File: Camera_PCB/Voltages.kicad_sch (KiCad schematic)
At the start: 29 parts

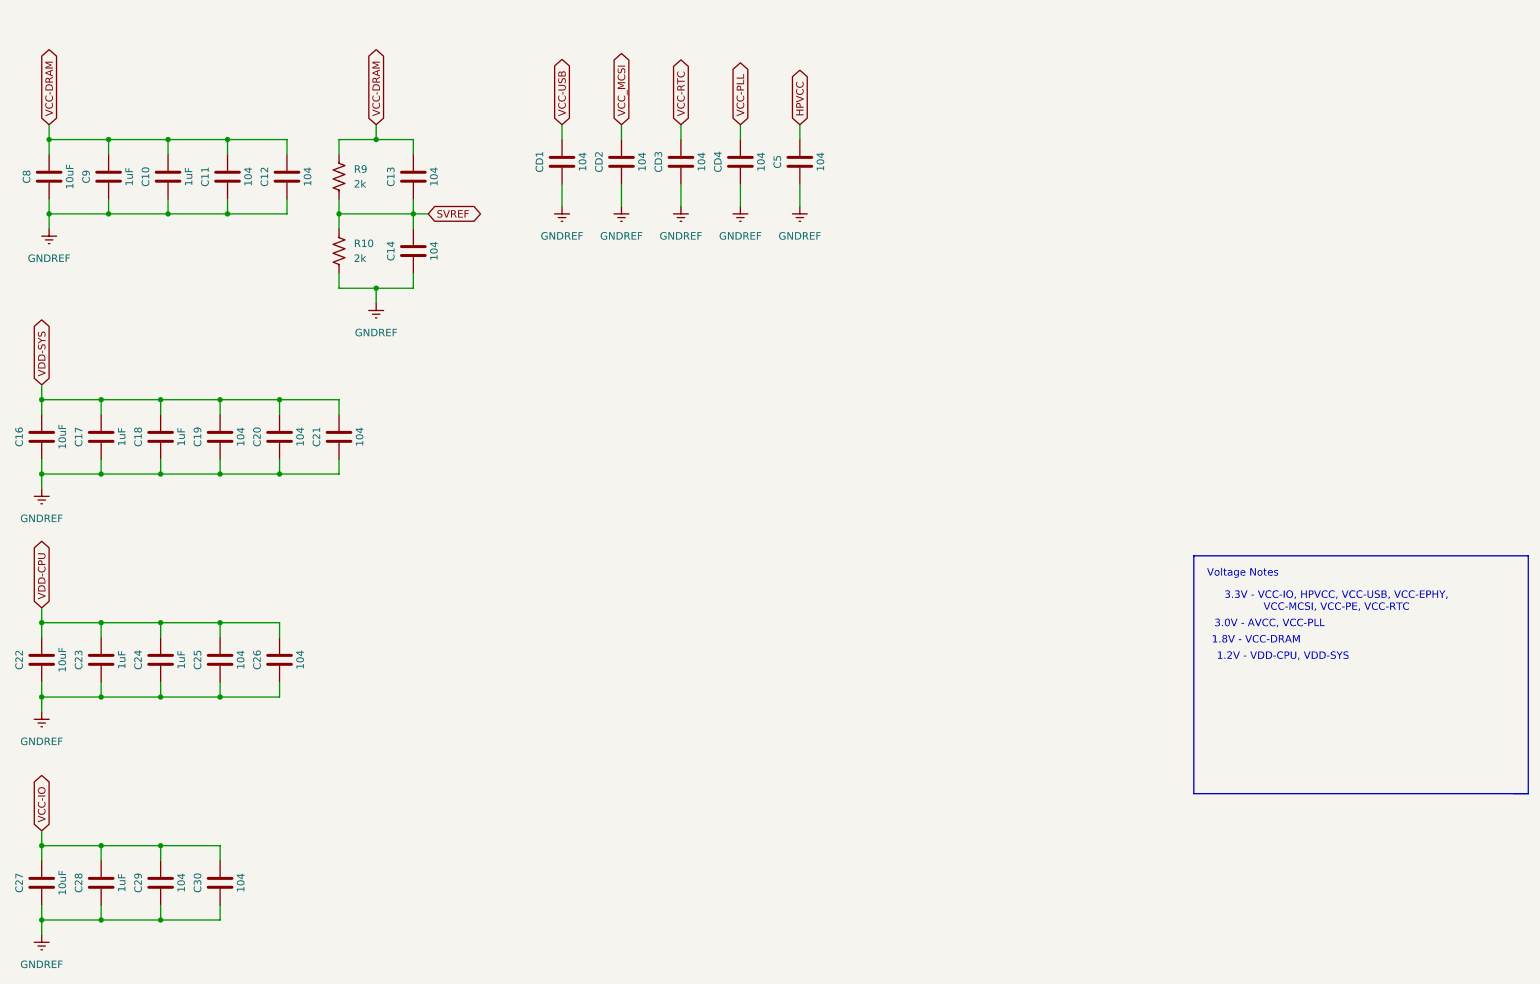
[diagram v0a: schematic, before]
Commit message: Fixed Capacitor Naming
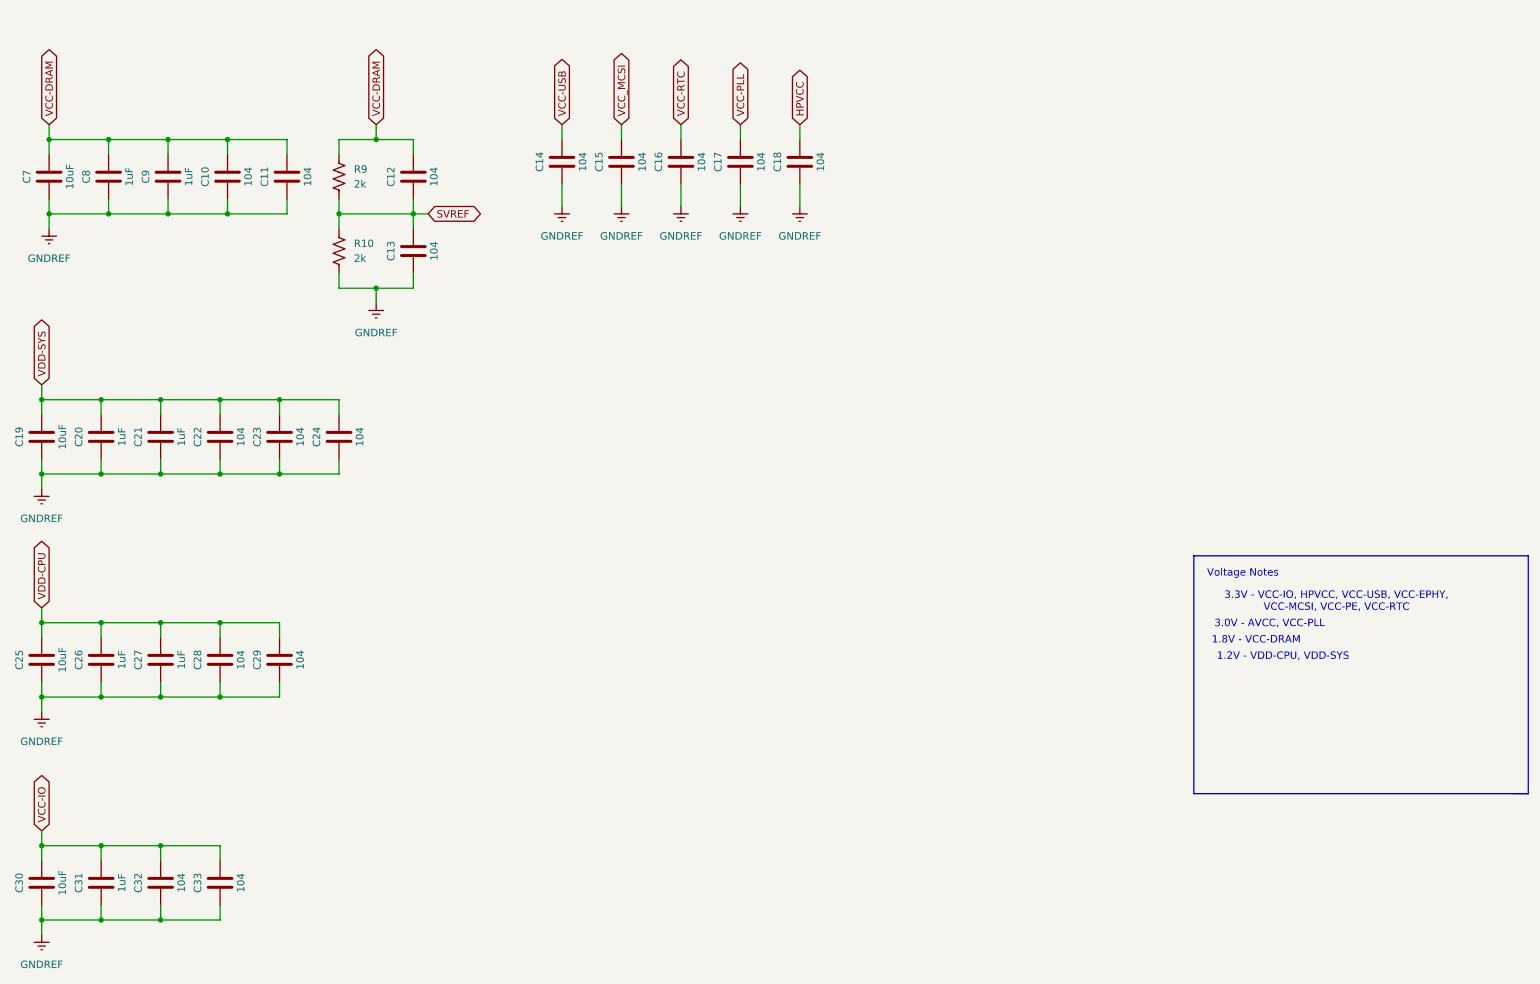
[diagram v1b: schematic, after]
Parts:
- renumbered C11 to C10, C12 to C11, C13 to C12, C14 to C13, CD1 to C14, CD2 to C15, CD3 to C16, CD4 to C17, C5 to C18, C16 to C19, C17 to C20, C18 to C21, C19 to C22, C20 to C23, C21 to C24, C22 to C25, C23 to C26, C24 to C27, C25 to C28, C26 to C29, C27 to C30, C28 to C31, C29 to C32, C30 to C33, C8 to C7, C9 to C8, C10 to C9
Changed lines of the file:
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@@
 		(on_board yes)
 		(dnp no)
-		(property "Reference" "C17"
+		(property "Reference" "C20"
 			(at 30.48 100.33 90)
 			(effects
@@
 			(project "Camera_PCB"
 				(path "/400c1603-202c-4359-a830-d2f0d06dd3ce/8aea63de-025a-40df-acd1-ce0de9a2cf46"
-					(reference "C17")
+					(reference "C20")
 					(unit 1)
 				)
@@
 		(on_board yes)
 		(dnp no)
-		(property "Reference" "CD1"
+		(property "Reference" "C14"
 			(at 109.22 53.34 90)
 			(effects
@@
 			(project "Camera_PCB"
 				(path "/400c1603-202c-4359-a830-d2f0d06dd3ce/8aea63de-025a-40df-acd1-ce0de9a2cf46"
-					(reference "CD1")
+					(reference "C14")
 					(unit 1)
 				)
@@
 		(on_board yes)
 		(dnp no)
-		(property "Reference" "C29"
+		(property "Reference" "C32"
 			(at 40.64 176.53 90)
 			(effects
@@
 			(project "Camera_PCB"
 				(path "/400c1603-202c-4359-a830-d2f0d06dd3ce/8aea63de-025a-40df-acd1-ce0de9a2cf46"
-					(reference "C29")
+					(reference "C32")
 					(unit 1)
 				)
@@
 		(on_board yes)
 		(dnp no)
-		(property "Reference" "C14"
+		(property "Reference" "C13"
 			(at 83.82 68.58 90)
 			(effects
@@
 			(project "Camera_PCB"
 				(path "/400c1603-202c-4359-a830-d2f0d06dd3ce/8aea63de-025a-40df-acd1-ce0de9a2cf46"
-					(reference "C14")
+					(reference "C13")
 					(unit 1)
 				)
@@
 		(on_board yes)
 		(dnp no)
-		(property "Reference" "C28"
+		(property "Reference" "C31"
 			(at 30.48 176.53 90)
 			(effects
@@
 			(project "Camera_PCB"
 				(path "/400c1603-202c-4359-a830-d2f0d06dd3ce/8aea63de-025a-40df-acd1-ce0de9a2cf46"
-					(reference "C28")
+					(reference "C31")
 					(unit 1)
 				)
@@
 		(on_board yes)
 		(dnp no)
-		(property "Reference" "CD4"
+		(property "Reference" "C17"
 			(at 139.7 53.34 90)
 			(effects
@@
 			(project "Camera_PCB"
 				(path "/400c1603-202c-4359-a830-d2f0d06dd3ce/8aea63de-025a-40df-acd1-ce0de9a2cf46"
-					(reference "CD4")
+					(reference "C17")
 					(unit 1)
 				)
@@
 		(on_board yes)
 		(dnp no)
-		(property "Reference" "C11"
+		(property "Reference" "C10"
 			(at 52.07 55.88 90)
 			(effects
@@
 			(project "Camera_PCB"
 				(path "/400c1603-202c-4359-a830-d2f0d06dd3ce/8aea63de-025a-40df-acd1-ce0de9a2cf46"
-					(reference "C11")
+					(reference "C10")
 					(unit 1)
 				)
@@
 		(on_board yes)
 		(dnp no)
-		(property "Reference" "C22"
+		(property "Reference" "C25"
 			(at 20.32 138.43 90)
 			(effects
@@
 			(project "Camera_PCB"
 				(path "/400c1603-202c-4359-a830-d2f0d06dd3ce/8aea63de-025a-40df-acd1-ce0de9a2cf46"
-					(reference "C22")
+					(reference "C25")
 					(unit 1)
 				)
@@
 		(on_board yes)
 		(dnp no)
-		(property "Reference" "C30"
+		(property "Reference" "C33"
 			(at 50.8 176.53 90)
 			(effects
@@
 			(project "Camera_PCB"
 				(path "/400c1603-202c-4359-a830-d2f0d06dd3ce/8aea63de-025a-40df-acd1-ce0de9a2cf46"
-					(reference "C30")
+					(reference "C33")
 					(unit 1)
 				)
@@
 		(on_board yes)
 		(dnp no)
-		(property "Reference" "C24"
+		(property "Reference" "C27"
 			(at 40.64 138.43 90)
 			(effects
@@
 			(project "Camera_PCB"
 				(path "/400c1603-202c-4359-a830-d2f0d06dd3ce/8aea63de-025a-40df-acd1-ce0de9a2cf46"
-					(reference "C24")
+					(reference "C27")
 					(unit 1)
 				)
@@
 		(on_board yes)
 		(dnp no)
-		(property "Reference" "C23"
+		(property "Reference" "C26"
 			(at 30.48 138.43 90)
 			(effects
@@
 			(project "Camera_PCB"
 				(path "/400c1603-202c-4359-a830-d2f0d06dd3ce/8aea63de-025a-40df-acd1-ce0de9a2cf46"
-					(reference "C23")
+					(reference "C26")
 					(unit 1)
 				)
@@
 		(on_board yes)
 		(dnp no)
-		(property "Reference" "C10"
+		(property "Reference" "C9"
 			(at 41.91 55.88 90)
 			(effects
@@
 			(project "Camera_PCB"
 				(path "/400c1603-202c-4359-a830-d2f0d06dd3ce/8aea63de-025a-40df-acd1-ce0de9a2cf46"
-					(reference "C10")
+					(reference "C9")
 					(unit 1)
 				)
@@
 		(on_board yes)
 		(dnp no)
-		(property "Reference" "CD2"
+		(property "Reference" "C15"
 			(at 119.38 53.34 90)
 			(effects
@@
 			(project "Camera_PCB"
 				(path "/400c1603-202c-4359-a830-d2f0d06dd3ce/8aea63de-025a-40df-acd1-ce0de9a2cf46"
-					(reference "CD2")
+					(reference "C15")
 					(unit 1)
 				)
@@
 		(on_board yes)
 		(dnp no)
-		(property "Reference" "C9"
+		(property "Reference" "C8"
 			(at 31.75 55.88 90)
 			(effects
@@
 			(project "Camera_PCB"
 				(path "/400c1603-202c-4359-a830-d2f0d06dd3ce/8aea63de-025a-40df-acd1-ce0de9a2cf46"
-					(reference "C9")
+					(reference "C8")
 					(unit 1)
 				)
@@
 		(on_board yes)
 		(dnp no)
-		(property "Reference" "C26"
+		(property "Reference" "C29"
 			(at 60.96 138.43 90)
 			(effects
@@
 			(project "Camera_PCB"
 				(path "/400c1603-202c-4359-a830-d2f0d06dd3ce/8aea63de-025a-40df-acd1-ce0de9a2cf46"
-					(reference "C26")
+					(reference "C29")
 					(unit 1)
 				)
@@
 		(on_board yes)
 		(dnp no)
-		(property "Reference" "C21"
+		(property "Reference" "C24"
 			(at 71.12 100.33 90)
 			(effects
@@
 			(project "Camera_PCB"
 				(path "/400c1603-202c-4359-a830-d2f0d06dd3ce/8aea63de-025a-40df-acd1-ce0de9a2cf46"
-					(reference "C21")
+					(reference "C24")
 					(unit 1)
 				)
@@
 		(on_board yes)
 		(dnp no)
-		(property "Reference" "C18"
+		(property "Reference" "C21"
 			(at 40.64 100.33 90)
 			(effects
@@
 			(project "Camera_PCB"
 				(path "/400c1603-202c-4359-a830-d2f0d06dd3ce/8aea63de-025a-40df-acd1-ce0de9a2cf46"
-					(reference "C18")
+					(reference "C21")
 					(unit 1)
 				)
@@
 		(on_board yes)
 		(dnp no)
-		(property "Reference" "CD3"
+		(property "Reference" "C16"
 			(at 129.54 53.34 90)
 			(effects
@@
 			(project "Camera_PCB"
 				(path "/400c1603-202c-4359-a830-d2f0d06dd3ce/8aea63de-025a-40df-acd1-ce0de9a2cf46"
-					(reference "CD3")
+					(reference "C16")
 					(unit 1)
 				)
@@
 		(on_board yes)
 		(dnp no)
-		(property "Reference" "C19"
+		(property "Reference" "C22"
 			(at 50.8 100.33 90)
 			(effects
@@
 			(project "Camera_PCB"
 				(path "/400c1603-202c-4359-a830-d2f0d06dd3ce/8aea63de-025a-40df-acd1-ce0de9a2cf46"
-					(reference "C19")
+					(reference "C22")
 					(unit 1)
 				)
@@
 		(on_board yes)
 		(dnp no)
-		(property "Reference" "C16"
+		(property "Reference" "C19"
 			(at 20.32 100.33 90)
 			(effects
@@
 			(project "Camera_PCB"
 				(path "/400c1603-202c-4359-a830-d2f0d06dd3ce/8aea63de-025a-40df-acd1-ce0de9a2cf46"
-					(reference "C16")
+					(reference "C19")
 					(unit 1)
 				)
@@
 		(on_board yes)
 		(dnp no)
-		(property "Reference" "C13"
+		(property "Reference" "C12"
 			(at 83.82 55.88 90)
 			(effects
@@
 			(project "Camera_PCB"
 				(path "/400c1603-202c-4359-a830-d2f0d06dd3ce/8aea63de-025a-40df-acd1-ce0de9a2cf46"
-					(reference "C13")
+					(reference "C12")
 					(unit 1)
 				)
@@
 		(on_board yes)
 		(dnp no)
-		(property "Reference" "C5"
+		(property "Reference" "C18"
 			(at 149.86 53.34 90)
 			(effects
@@
 			(project "Camera_PCB"
 				(path "/400c1603-202c-4359-a830-d2f0d06dd3ce/8aea63de-025a-40df-acd1-ce0de9a2cf46"
-					(reference "C5")
+					(reference "C18")
 					(unit 1)
 				)
@@
 		(on_board yes)
 		(dnp no)
-		(property "Reference" "C25"
+		(property "Reference" "C28"
 			(at 50.8 138.43 90)
 			(effects
@@
 			(project "Camera_PCB"
 				(path "/400c1603-202c-4359-a830-d2f0d06dd3ce/8aea63de-025a-40df-acd1-ce0de9a2cf46"
-					(reference "C25")
+					(reference "C28")
 					(unit 1)
 				)
@@
 		(on_board yes)
 		(dnp no)
-		(property "Reference" "C12"
+		(property "Reference" "C11"
 			(at 62.23 55.88 90)
 			(effects
@@
 			(project "Camera_PCB"
 				(path "/400c1603-202c-4359-a830-d2f0d06dd3ce/8aea63de-025a-40df-acd1-ce0de9a2cf46"
-					(reference "C12")
+					(reference "C11")
 					(unit 1)
 				)
@@
 		(on_board yes)
 		(dnp no)
-		(property "Reference" "C27"
+		(property "Reference" "C30"
 			(at 20.32 176.53 90)
 			(effects
@@
 			(project "Camera_PCB"
 				(path "/400c1603-202c-4359-a830-d2f0d06dd3ce/8aea63de-025a-40df-acd1-ce0de9a2cf46"
-					(reference "C27")
+					(reference "C30")
 					(unit 1)
 				)
@@
 		(on_board yes)
 		(dnp no)
-		(property "Reference" "C8"
+		(property "Reference" "C7"
 			(at 21.59 55.88 90)
 			(effects
@@
 			(project "Camera_PCB"
 				(path "/400c1603-202c-4359-a830-d2f0d06dd3ce/8aea63de-025a-40df-acd1-ce0de9a2cf46"
-					(reference "C8")
+					(reference "C7")
 					(unit 1)
 				)
@@
 		(on_board yes)
 		(dnp no)
-		(property "Reference" "C20"
+		(property "Reference" "C23"
 			(at 60.96 100.33 90)
 			(effects
@@
 			(project "Camera_PCB"
 				(path "/400c1603-202c-4359-a830-d2f0d06dd3ce/8aea63de-025a-40df-acd1-ce0de9a2cf46"
-					(reference "C20")
-					(unit 1)
-				)
+					(reference "C23")
+					(unit 1)
+				)

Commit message: Camera connections added
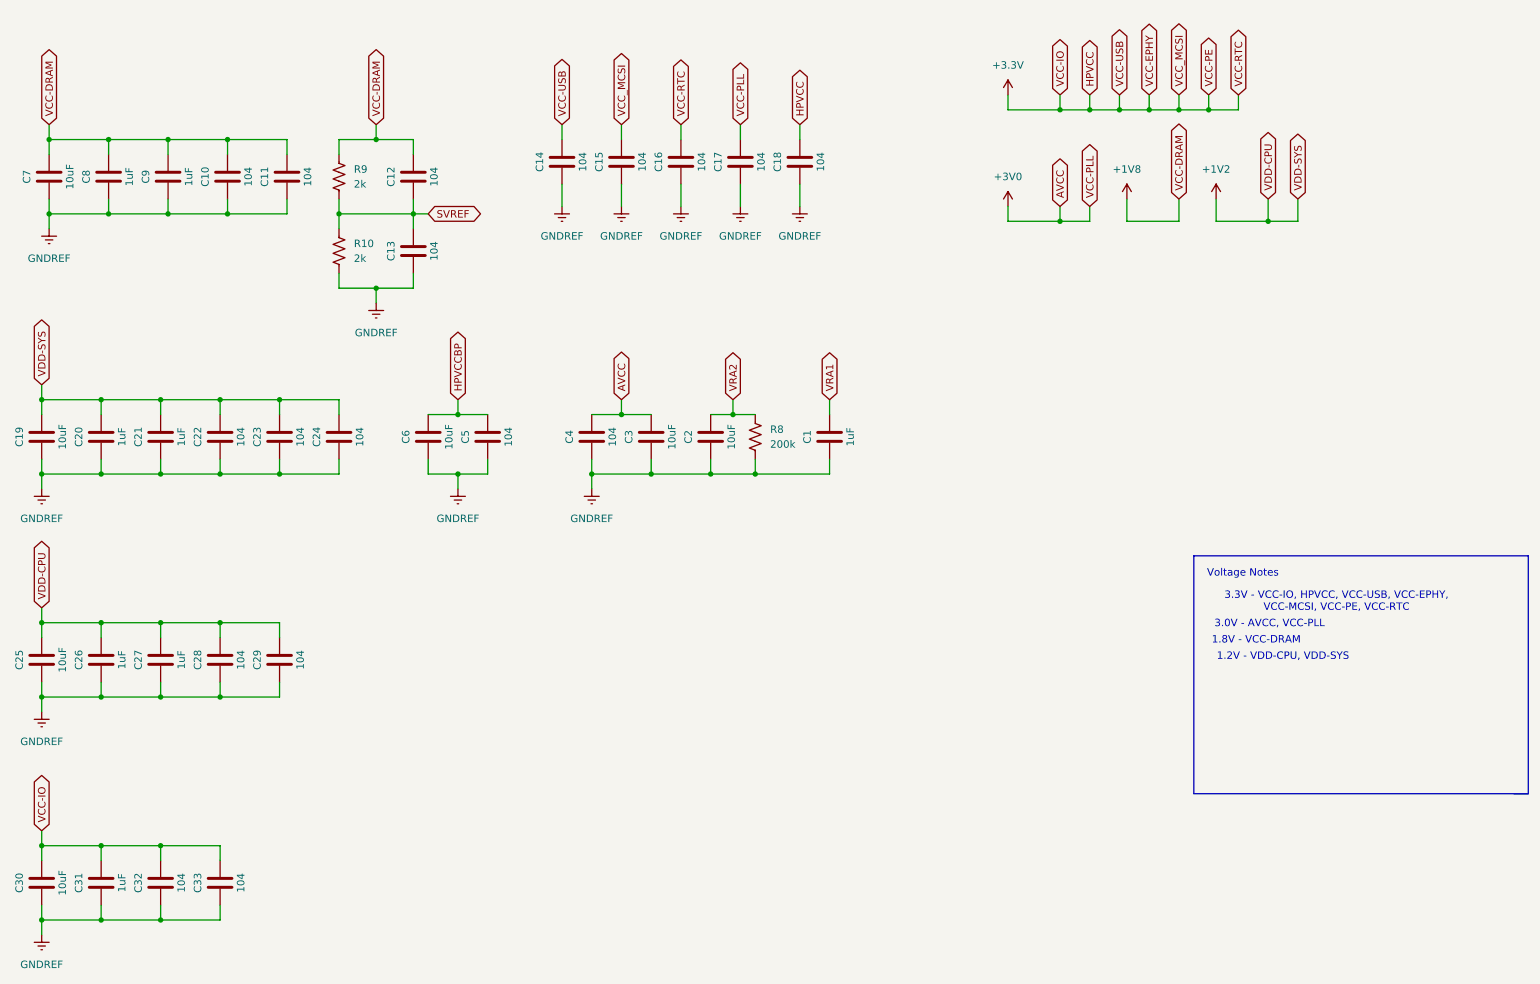
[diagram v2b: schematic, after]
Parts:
- added C1: 1uF, symbol Device:C
- added C2, C3, C6: 10uF, symbol Device:C
- added C4, C5: 104, symbol Device:C
- added R8: 200k, symbol Device:R_US
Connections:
- net VCC-IO is gone; now on net +3.3V: C30.2, C31.2, C32.2, C33.2
- net VCC-RTC is gone; now on net +3.3V: C16.2
- net VCC-USB is gone; now on net +3.3V: C14.2
- net VCC_MCSI is gone; now on net +3.3V: C15.2
- net VDD-SYS is gone; now on net +1V2: C19.2, C20.2, C21.2, C22.2, C23.2, C24.2
- net GNDREF: now also C1.1, C2.1, C3.1, C4.1, C5.1, C6.1, R8.2
- net HPVCC renamed +3.3V
- net VCC-DRAM renamed +1V8
- net VCC-PLL renamed +3V0
- net +3V0: now also C3.2, C4.2
- net VDD-CPU renamed +1V2
- new net HPVCCBP: C5.2, C6.2
- new net VRA1: C1.2
- new net VRA2: C2.2, R8.1

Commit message: Switched pins 86, 87
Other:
- company: (none) -> Group 25 Senior Design
- title: (none) -> Wireless Backup Camera - Encoder
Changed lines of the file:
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@@
 	(generator_version "9.0")
 	(paper "A4")
+	(title_block
+		(title "Wireless Backup Camera - Encoder")
+		(company "Group 25 Senior Design")
+	)
 	(text "3.0V - AVCC, VCC-PLL"
 		(exclude_from_sim no)
